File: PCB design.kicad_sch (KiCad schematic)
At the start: 6 parts, among them U2 LM7812_TO220

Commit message: Added pdf of datasheet switching regulator
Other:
- title: (none) -> FNAF0670-V0
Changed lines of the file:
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@@
 	(generator_version "10.0")
 	(paper "A4")
+	(title_block
+		(title "FNAF0670-V0")
+	)
 	(rectangle
 		(start 233.68 74.93)

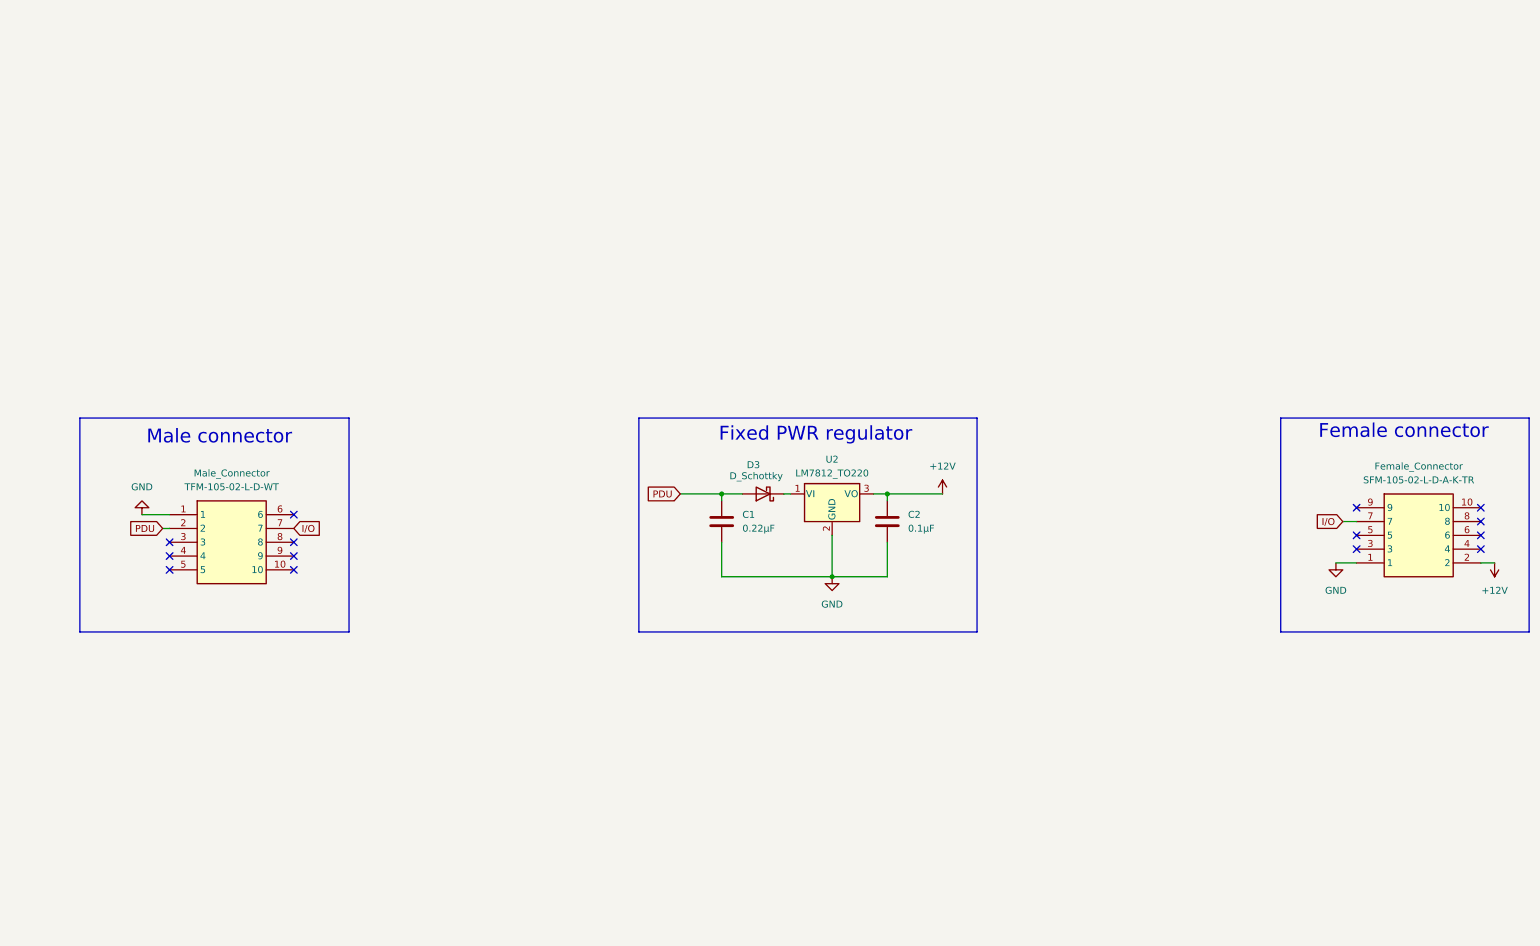
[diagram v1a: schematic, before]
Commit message: Added the symbol ecad to the schematics and started implementing the general circuit (im in wire-hell bcs the pins are placed differently from the d.s help
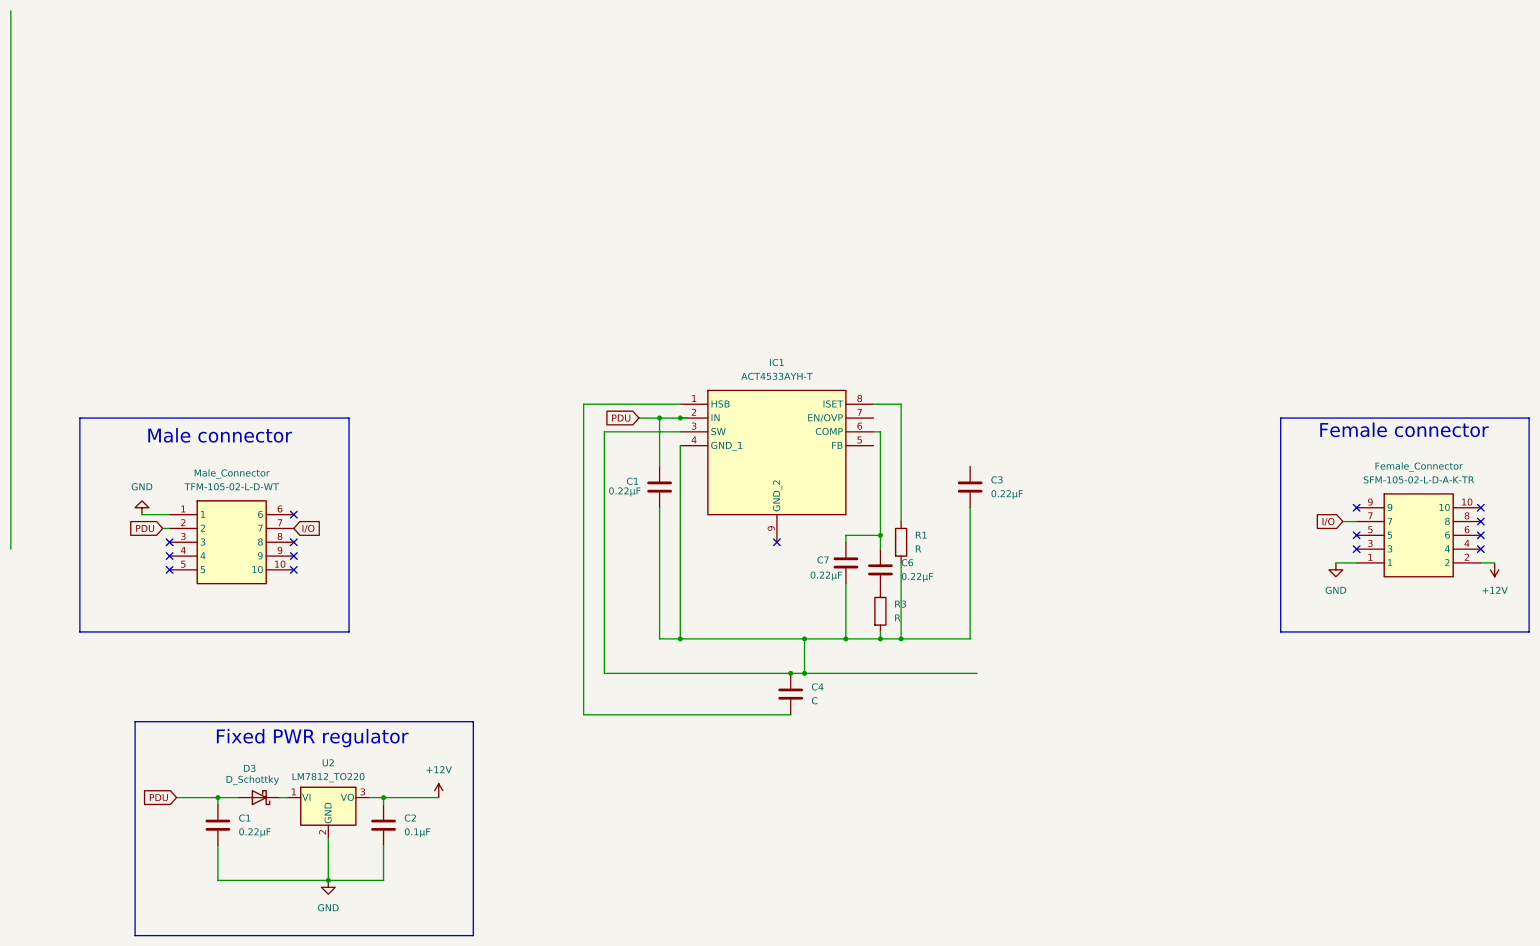
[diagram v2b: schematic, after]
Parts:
- added C1, C3, C6, C7: 0.22µF, symbol Device:C
- added C4: C, symbol Device:C
- added IC1: ACT4533AYH-T, SOIC127P600X170-9N, symbol ACT4533AYH-T:ACT4533AYH-T
- added R1, R3: R, symbol Device:R
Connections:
- net PDU: now also C1.1, IC1.2 (IN)
- new net: C6.1, C7.1, IC1.6 (COMP)
- new net: C1.2, C3.2, C4.1, C7.2, IC1.3 (SW), IC1.4 (GND_1), R1.2, R3.2
- new net: IC1.8 (ISET), R1.1
- new net: C6.2, R3.1
- new net: C4.2, IC1.1 (HSB)
- no-connect marks 14 -> 15
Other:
- moved on the sheet: C1, C2, D3, U2

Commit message: Added the completed schematics for switching regulator only, still need diode and capacitor
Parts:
- added D4: D_Schottky, Diode_SMD:D_0603_1608Metric, symbol Device:D_Schottky
- added L1: 40µH, symbol Device:L
- added R2: 10kΩ, symbol Device:R
- added R4, R5, R6: R, symbol Device:R
- C1: value 0.22µF -> 22µF
- C2: renamed from C6; value 0.22µF -> 10nF
- C3: renamed from C4; value C -> 22nF
- C4: renamed from C3; value 0.22µF -> 47µF
- C5: renamed from C7; value 0.22µF -> 100pF
- R1: value R -> 138.5kΩ
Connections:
- net +12V: now also C4.1, L1.2, R2.2, R5.2
- net at C1.2, C4.2, C5.2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: now also D4.1 (K), R4.2, R6.1; no longer C3.1, IC1.3 (SW)
- net at IC1.5 (FB): now also R2.1, R4.1
- net at IC1.7 (EN/OVP): now also R5.1, R6.2
- new net: C3.1, D4.2 (A), IC1.3 (SW), L1.1
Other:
- moved on the sheet: C1, C2, C3, C4, C5, R1, R3

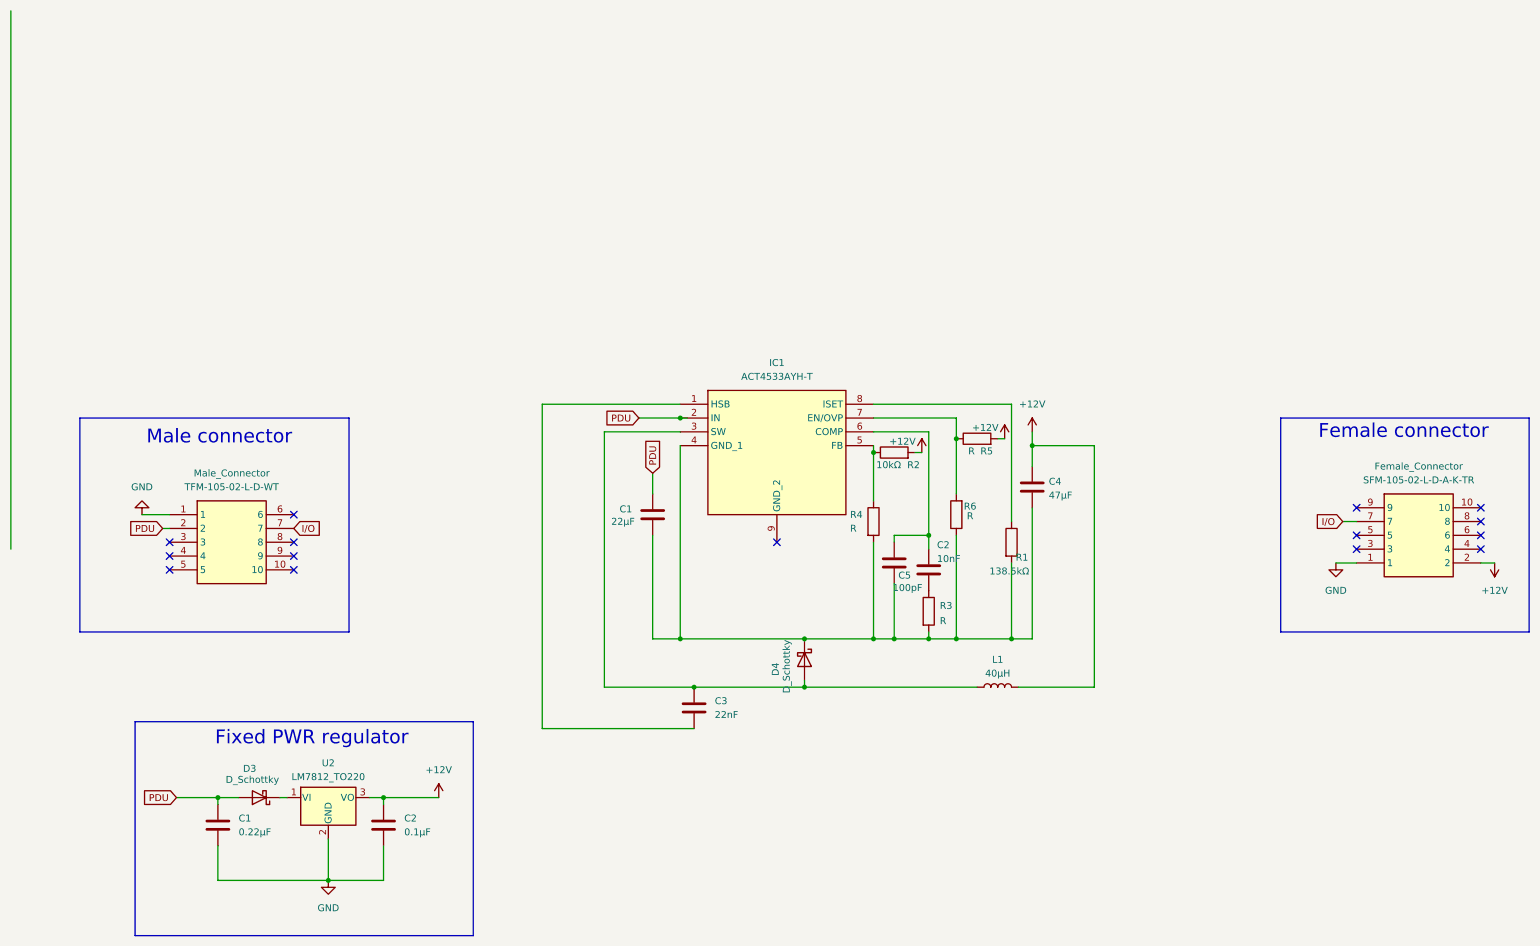
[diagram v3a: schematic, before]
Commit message: Added the R1 and R2 actual values for V_in = 12V
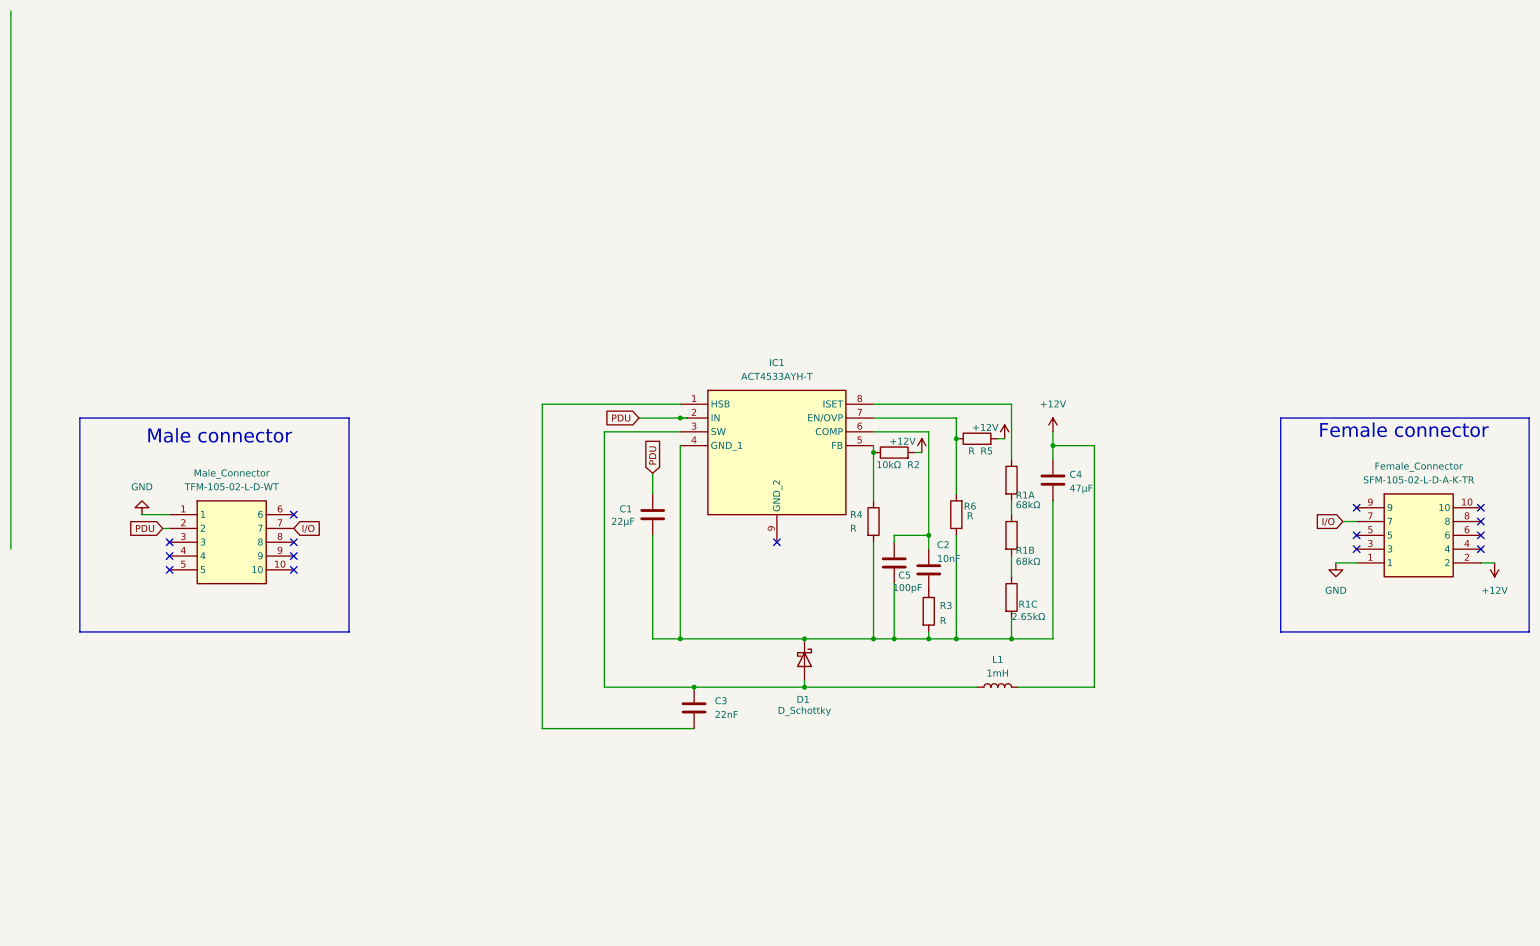
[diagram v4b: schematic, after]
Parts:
- removed C1: 0.22µF, symbol Device:C
- removed C2: 0.1µF, symbol Device:C
- removed D3: D_Schottky, Diode_SMD:D_0603_1608Metric, symbol Device:D_Schottky
- removed U2: LM7812_TO220, Package_TO_SOT_THT:TO-220-3_Vertical, symbol Regulator_Linear:LM7812_TO220
- added R1A: 68kΩ, symbol Device:R
- added R1C: 2.65kΩ, symbol Device:R
- L1: value 40µH -> 1mH
- R1B: renamed from R1; value 138.5kΩ -> 68kΩ
- renumbered D4 to D1
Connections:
- net at C1.2, C4.2, C5.2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: now also R1C.2; no longer R1B.2
- net at IC1.8 (ISET): now also R1A.1; no longer R1B.1
- new net: R1A.2, R1B.1
- new net: R1B.2, R1C.1
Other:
- note removed: "Fixed PWR regulator"
- moved on the sheet: C4, R1B

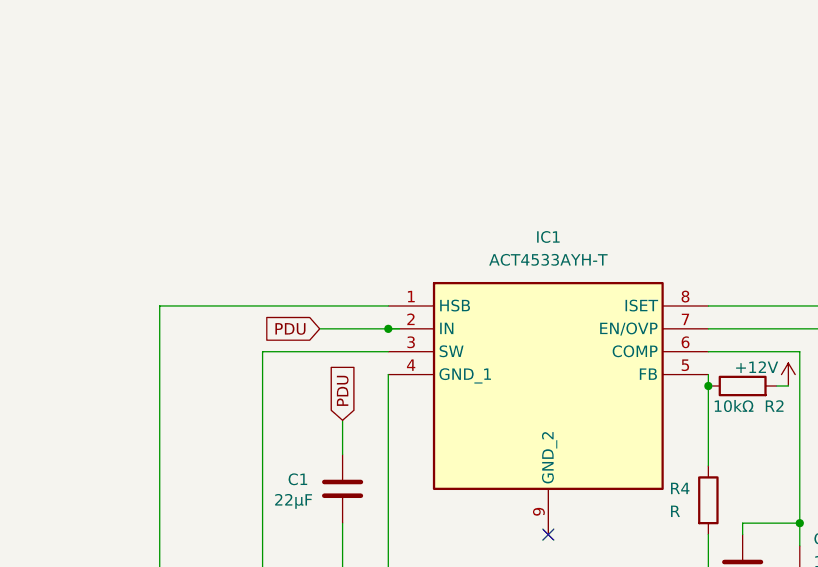
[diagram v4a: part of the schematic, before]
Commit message: Added name for the regulator, added a diode before the regulator and PDU tag for protection against reverse polarity, V_in from the PDU needs to be 12.V at least for the regulator to be able to work at V_in = 12V due to the voltage drop at the diode. I think C4 is the stabilizing capasitor. Will send this version to Sam for verification and ask for the rest of the resistor values
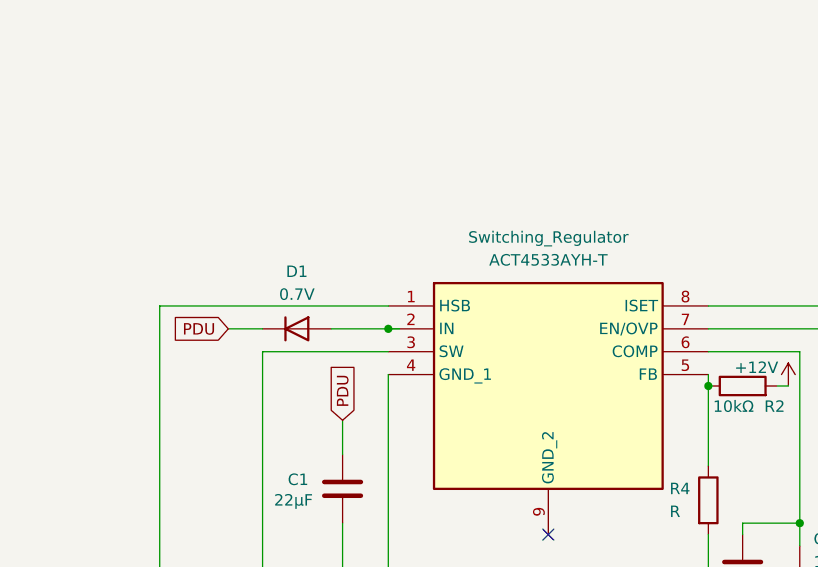
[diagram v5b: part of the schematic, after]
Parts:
- added D1: 0.7V, symbol Device:D
- renumbered IC1 to Switching_Regulator
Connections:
- net PDU: now also D1.1 (K); no longer Switching_Regulator.2 (IN)
- new net: D1.2 (A), Switching_Regulator.2 (IN)
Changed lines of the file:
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@@
+	)
+	(junction
+		(at 123.19 74.93)
+		(diameter 0)
+		(color 0 0 0 0)
 	)
 	(junction
@@
 	)
 	(junction
-		(at 123.19 74.93)
-		(diameter 0)
-		(color 0 0 0 0)
-	)
-	(junction
 		(at 162.56 115.57)
 		(diameter 0)
@@
 	(wire
 		(pts
-			(xy 115.57 74.93) (xy 123.19 74.93)
+			(xy 105.41 74.93) (xy 109.22 74.93)
 		)
 		(stroke
@@
 		(pts
 			(xy 184.15 115.57) (xy 191.77 115.57)
+		)
+		(stroke
+			(width 0)
+			(type default)
+		)
+	)
+	(wire
+		(pts
+			(xy 116.84 74.93) (xy 123.19 74.93)
 		)
 		(stroke
@@
 	(global_label "PDU"
 		(shape input)
-		(at 115.57 74.93 180)
+		(at 105.41 74.93 180)
 		(fields_autoplaced yes)
 		(effects
@@
 		)
 		(property "Intersheetrefs" "${INTERSHEET_REFS}"
-			(at 108.7143 74.93 0)
+			(at 98.5543 74.93 0)
 			(hide yes)
 			(show_name no)
@@
 	)
 	(symbol
+		(lib_id "Device:D")
+		(at 113.03 74.93 0)
+		(unit 1)
+		(body_style 1)
+		(exclude_from_sim no)
+		(in_bom yes)
+		(on_board yes)
+		(in_pos_files yes)
+		(dnp no)
+		(fields_autoplaced yes)
+		(property "Reference" "D1"
+			(at 113.03 68.58 0)
+			(show_name no)
+			(do_not_autoplace no)
+			(effects
+				(font
+					(size 1.27 1.27)
+				)
+			)
+		)
+		(property "Value" "0.7V"
+			(at 113.03 71.12 0)
+			(show_name no)
+			(do_not_autoplace no)
+			(effects
+				(font
+					(size 1.27 1.27)
+				)
+			)
+		)
+		(property "Footprint" ""
+			(at 113.03 74.93 0)
+			(hide yes)
+			(show_name no)
+			(do_not_autoplace no)
+			(effects
+				(font
+					(size 1.27 1.27)
+				)
+			)
+		)
+		(property "Datasheet" ""
+			(at 113.03 74.93 0)
+			(hide yes)
+			(show_name no)
+			(do_not_autoplace no)
+			(effects
+				(font
+					(size 1.27 1.27)
+				)
+			)
+		)
+		(property "Description" "Diode"
+			(at 113.03 74.93 0)
+			(hide yes)
+			(show_name no)
+			(do_not_autoplace no)
+			(effects
+				(font
+					(size 1.27 1.27)
+				)
+			)
+		)
+		(property "Sim.Device" "D"
+			(at 113.03 74.93 0)
+			(hide yes)
+			(show_name no)
+			(do_not_autoplace no)
+			(effects
+				(font
+					(size 1.27 1.27)
+				)
+			)
+		)
+		(property "Sim.Pins" "1=K 2=A"
+			(at 113.03 74.93 0)
+			(hide yes)
+			(show_name no)
+			(do_not_autoplace no)
+			(effects
+				(font
+					(size 1.27 1.27)
+				)
+			)
+		)
+		(pin "2"
+		)
+		(pin "1"
+		)
+		(instances
+			(project "PCB design"
+				(path "/1ee13f0d-22f2-4352-9e68-759581f4b836"
+					(reference "D1")
+					(unit 1)
+				)
+			)
+		)
+	)
+	(symbol
 		(lib_id "Device:C")
 		(at 191.77 86.36 0)
@@
 		(dnp no)
 		(fields_autoplaced yes)
-		(property "Reference" "IC1"
+		(property "Reference" "Switching_Regulator"
 			(at 140.97 64.77 0)
 			(show_name no)
@@
 			(project "PCB design"
 				(path "/1ee13f0d-22f2-4352-9e68-759581f4b836"
-					(reference "IC1")
+					(reference "Switching_Regulator")
 					(unit 1)
 				)
